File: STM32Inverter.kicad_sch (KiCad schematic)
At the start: 100 parts, among them J1 STLINK, J2 CURRENT SENSE, J5 UART, J6 INTERFACE, J7 POWER, J8 501571-2007, J9 RESOLVER, Q4 ST3422A, U1 STM32F303VCTx, U10 ULN2002, U11 LM393, U12 LM393, U4 74HCT00, U7 MCP2551-I-SN, Y3 CSTNE8M00GH5C000R0

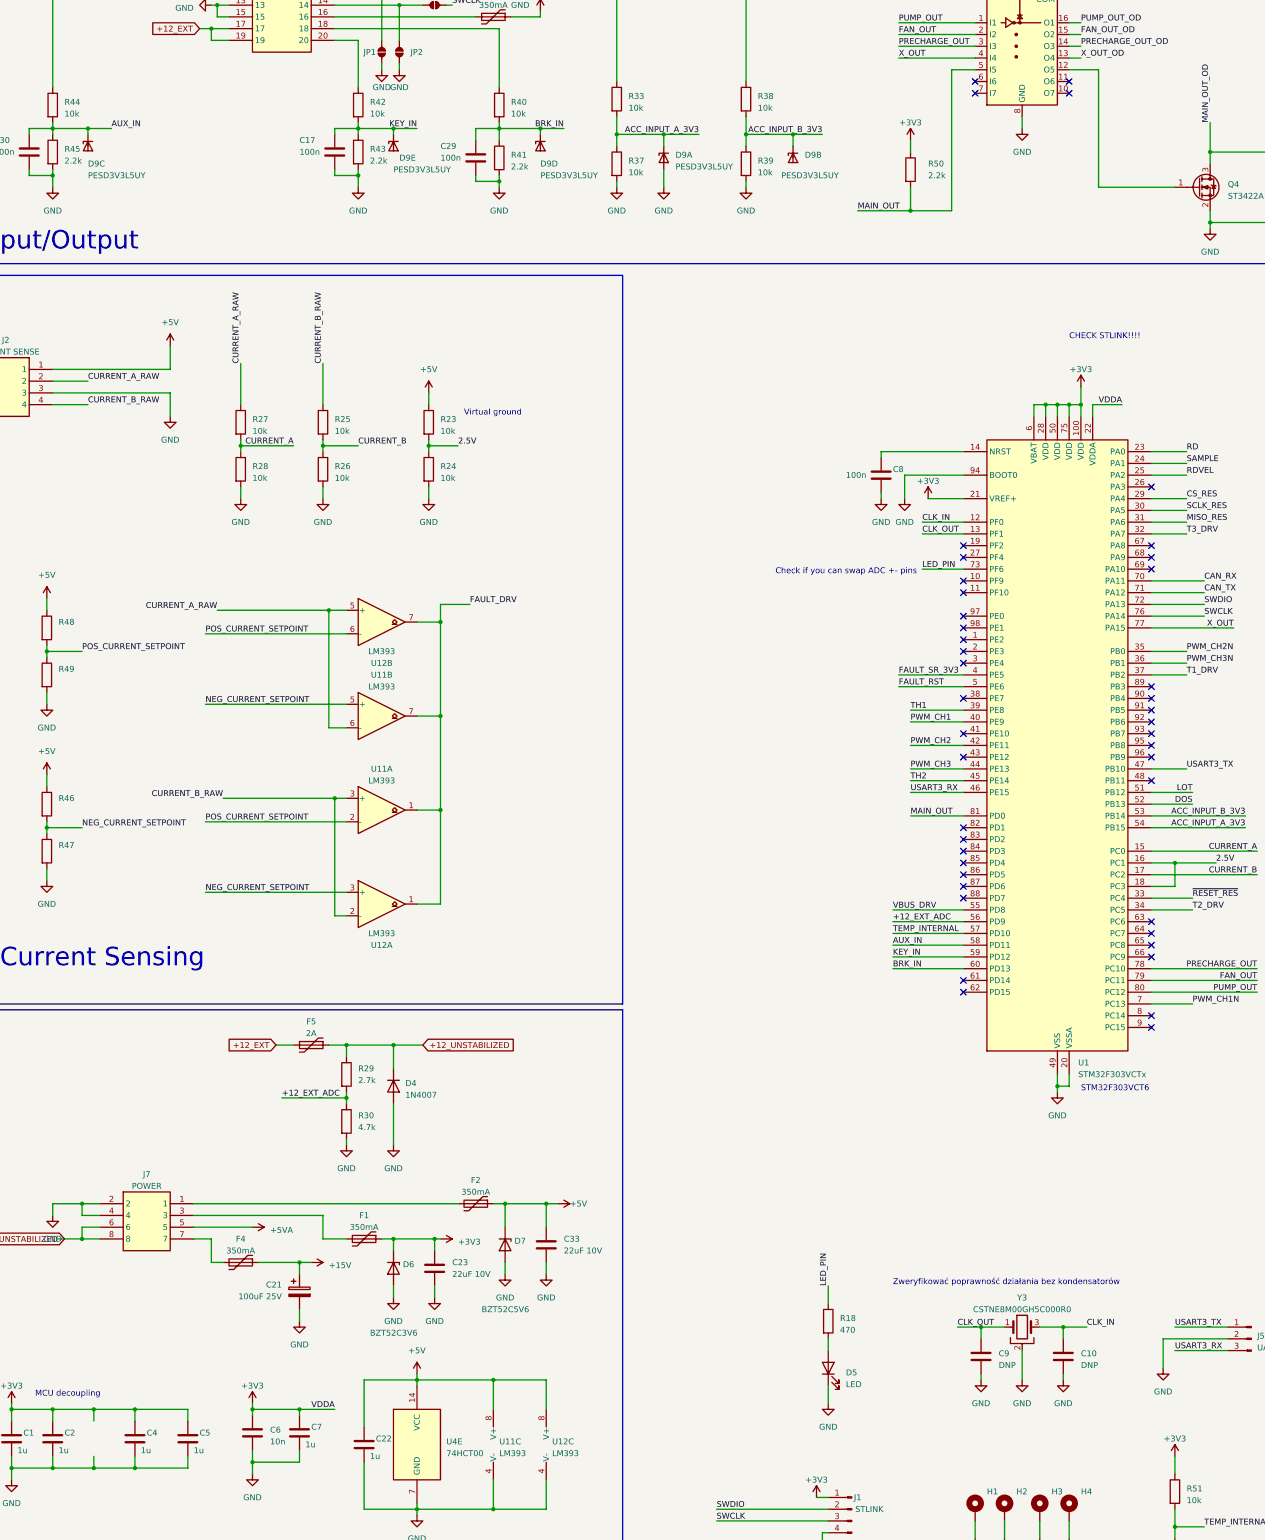
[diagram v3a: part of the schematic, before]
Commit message: Added mosfet pullup to +5V
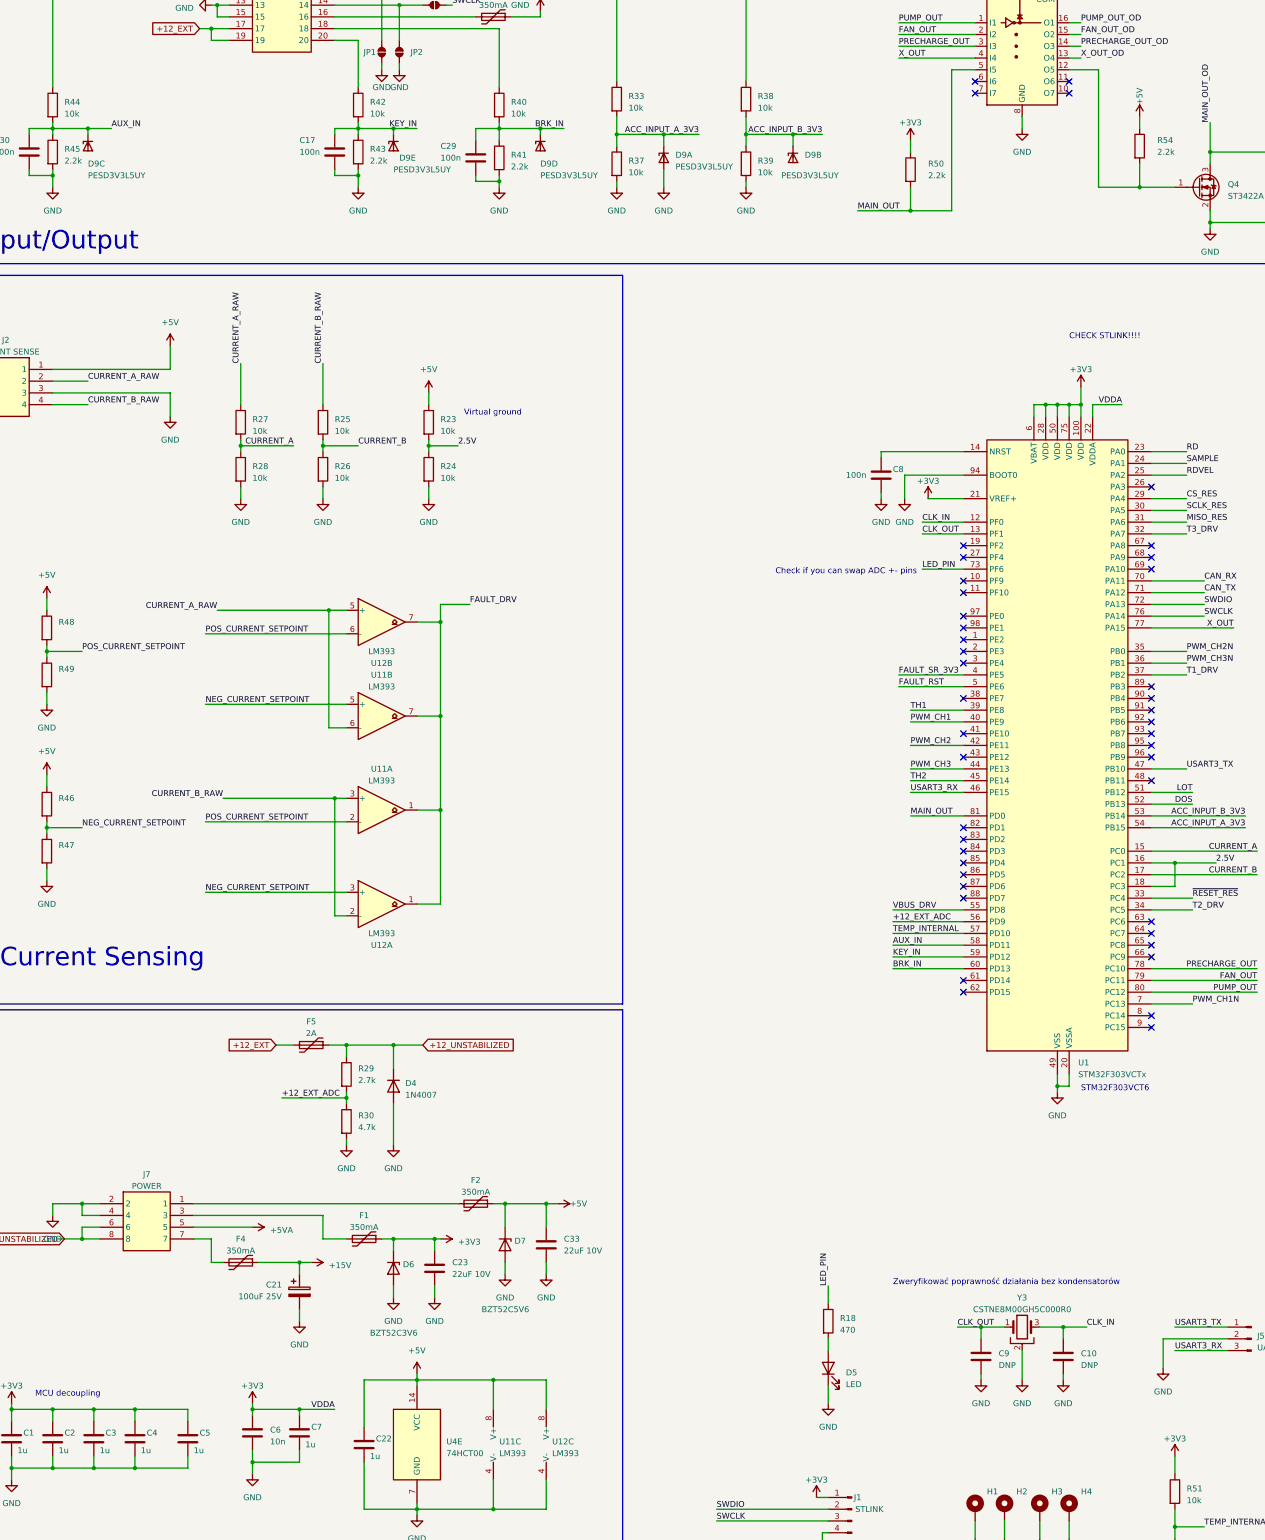
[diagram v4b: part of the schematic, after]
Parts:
- added C3: 1u, Capacitor_SMD:C_0402_1005Metric_Pad0.74x0.62mm_HandSolder, symbol Device:C
- added R54: 2.2k, Resistor_SMD:R_0603_1608Metric_Pad0.98x0.95mm_HandSolder, symbol Device:R
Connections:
- net +3V3: now also C3.1
- net +5V: now also R54.1
- net GND: now also C3.2
- net at Q4.1 (G), U10.12 (O5): now also R54.2
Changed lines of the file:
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@@
   (junction (at 95.25 137.16) (diameter 0) (color 0 0 0 0)
   )
+  (junction (at 271.78 81.28) (diameter 0) (color 0 0 0 0)
+  )
   (junction (at 254 128.27) (diameter 0) (color 0 0 0 0)
   )
@@
     (stroke (width 0) (type default))
   )
+  (wire (pts (xy 271.78 76.2) (xy 271.78 81.28))
+    (stroke (width 0) (type default))
+  )
   (wire (pts (xy 246.38 66.04) (xy 246.38 68.58))
     (stroke (width 0) (type default))
@@
     (stroke (width 0) (type default))
   )
-  (wire (pts (xy 279.4 81.28) (xy 262.89 81.28))
+  (wire (pts (xy 279.4 81.28) (xy 271.78 81.28))
     (stroke (width 0) (type default))
   )
@@
     (stroke (width 0) (type default))
   )
+  (wire (pts (xy 271.78 66.04) (xy 271.78 68.58))
+    (stroke (width 0) (type default))
+  )
   (wire (pts (xy 224.79 156.21) (xy 233.68 156.21))
     (stroke (width 0) (type default))
@@
     (stroke (width 0) (type default))
   )
+  (wire (pts (xy 271.78 81.28) (xy 262.89 81.28))
+    (stroke (width 0) (type default))
+  )
   (wire (pts (xy 46.99 306.07) (xy 43.18 306.07))
     (stroke (width 0) (type default))
@@
     )
   )
+  (symbol (lib_id "power:+5V") (at 271.78 66.04 0) (unit 1)
+    (in_bom yes) (on_board yes) (dnp no)
+    (property "Reference" "#PWR0111" (at 271.78 69.85 0)
+      (effects (font (size 1.27 1.27)) hide)
+    )
+    (property "Value" "+5V" (at 271.78 63.5 90)
+      (effects (font (size 1.27 1.27)) (justify left))
+    )
+    (property "Footprint" "" (at 271.78 66.04 0)
+      (effects (font (size 1.27 1.27)) hide)
+    )
+    (property "Datasheet" "" (at 271.78 66.04 0)
+      (effects (font (size 1.27 1.27)) hide)
+    )
+    (pin "1")
+    (instances
+      (project "STM32Inverter"
+        (path "/a3442e80-7eef-4b96-92a1-138eb3b79ccb"
+          (reference "#PWR0111") (unit 1)
+        )
+      )
+      (project "ecu"
+        (path "/d5e79731-82c5-4736-aeb7-96bb55f694f3"
+          (reference "#PWR014") (unit 1)
+        )
+      )
+    )
+  )
   (symbol (lib_id "power:GND") (at 254 276.86 0) (unit 1)
     (in_bom yes) (on_board yes) (dnp no) (fields_autoplaced)
@@
     )
   )
+  (symbol (lib_id "Device:R") (at 271.78 72.39 0) (unit 1)
+    (in_bom yes) (on_board yes) (dnp no)
+    (property "Reference" "R54" (at 275.59 71.12 0)
+      (effects (font (size 1.27 1.27)) (justify left))
+    )
+    (property "Value" "2.2k" (at 275.59 73.66 0)
+      (effects (font (size 1.27 1.27)) (justify left))
+    )
+    (property "Footprint" "Resistor_SMD:R_0603_1608Metric_Pad0.98x0.95mm_HandSolder" (at 270.002 72.39 90)
+      (effects (font (size 1.27 1.27)) hide)
+    )
+    (property "Datasheet" "~" (at 271.78 72.39 0)
+      (effects (font (size 1.27 1.27)) hide)
+    )
+    (pin "1")
+    (pin "2")
+    (instances
+      (project "STM32Inverter"
+        (path "/a3442e80-7eef-4b96-92a1-138eb3b79ccb"
+          (reference "R54") (unit 1)
+        )
+      )
+    )
+  )
   (symbol (lib_id "MEMS_Passive:SolderableJumper") (at 119.38 41.91 180) (unit 1)
     (in_bom yes) (on_board yes) (dnp no) (fields_autoplaced)
@@
         )
       )
+    )
+  )
+  (symbol (lib_id "Device:C") (at 45.72 351.79 0) (unit 1)
+    (in_bom yes) (on_board yes) (dnp no)
+    (property "Reference" "C3" (at 48.26 350.52 0)
+      (effects (font (size 1.27 1.27)) (justify left))
+    )
+    (property "Value" "1u" (at 46.99 354.33 0)
+      (effects (font (size 1.27 1.27)) (justify left))
+    )
+    (property "Footprint" "Capacitor_SMD:C_0402_1005Metric_Pad0.74x0.62mm_HandSolder" (at 46.6852 355.6 0)
+      (effects (font (size 1.27 1.27)) hide)
+    )
+    (property "Datasheet" "~" (at 45.72 351.79 0)
+      (effects (font (size 1.27 1.27)) hide)
+    )
+    (property "LCSC" "C126521" (at 45.72 351.79 0)
+      (effects (font (size 1.27 1.27)) hide)
+    )
+    (pin "1")
+    (pin "2")
+    (instances
+      (project "STM32Inverter"
+        (path "/a3442e80-7eef-4b96-92a1-138eb3b79ccb"
+          (reference "C3") (unit 1)
+        )
+      )
